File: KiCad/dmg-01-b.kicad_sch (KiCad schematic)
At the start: 64 parts, among them CN1 SCREEN, CN2 CART, CN3 EXT, P1 GND PAD, P2 GND PAD, P3 GND PAD, P4 GND PAD, SW1 POWER_SW, U1 CPU, U2 VRAM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

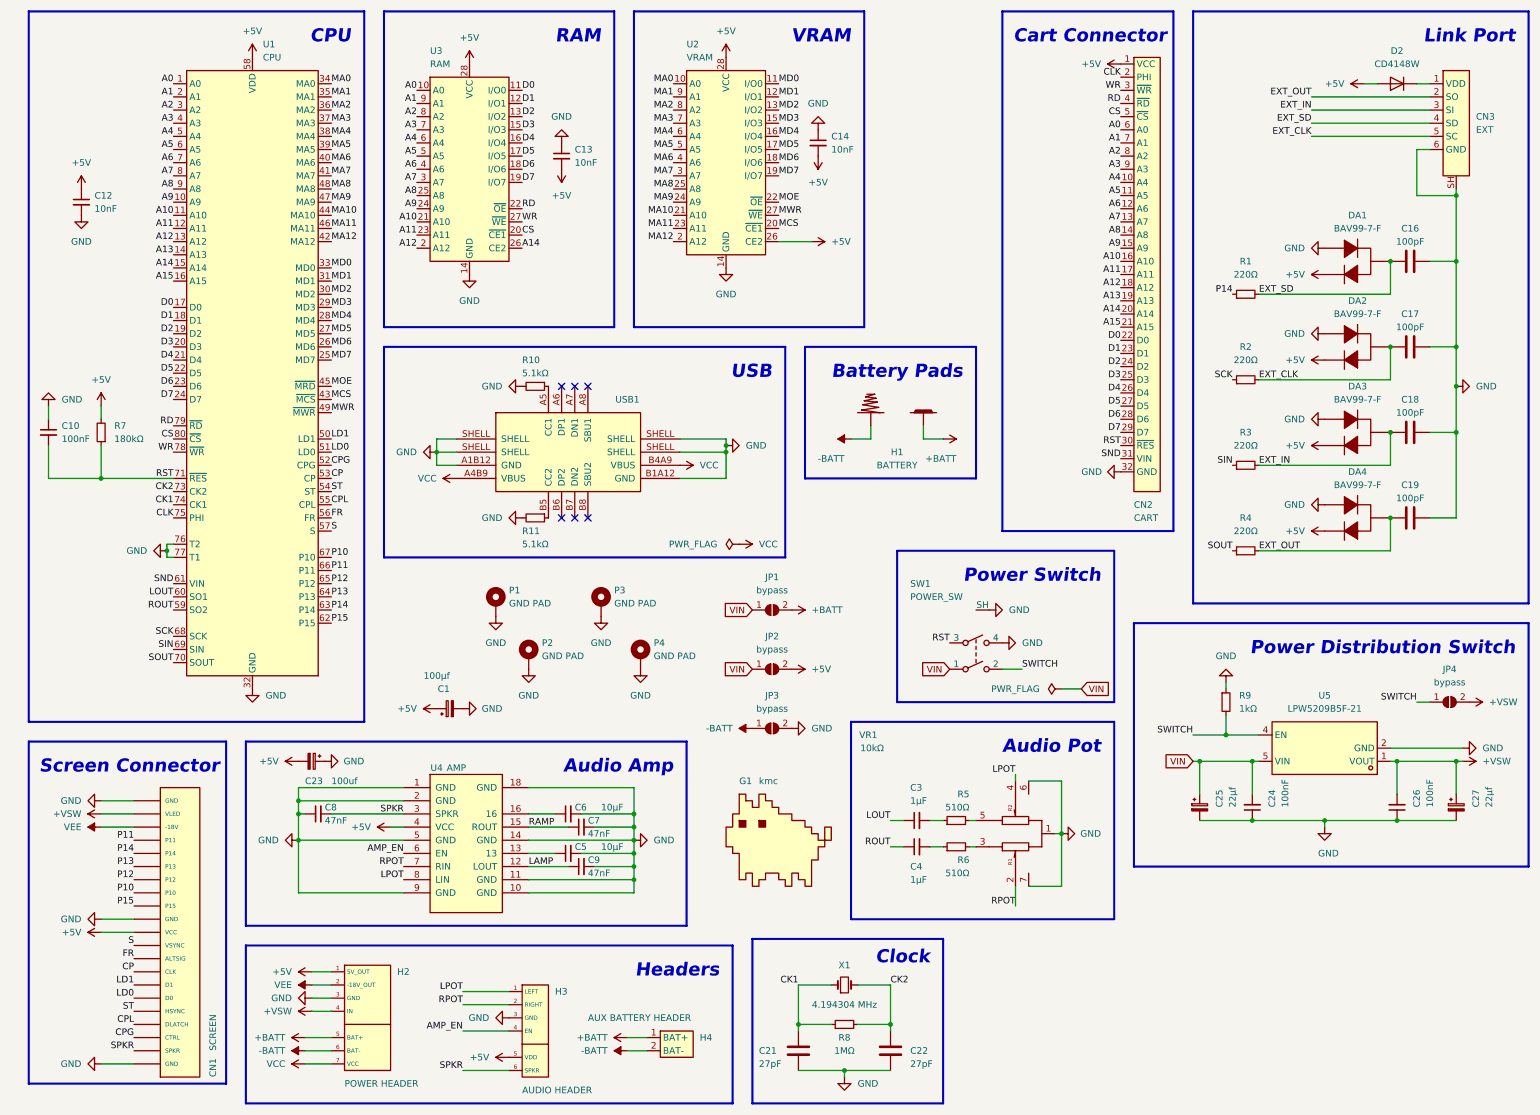
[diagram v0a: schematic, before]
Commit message: - fix c23 orientation - fix d2 footprint - minor silkscreen changes
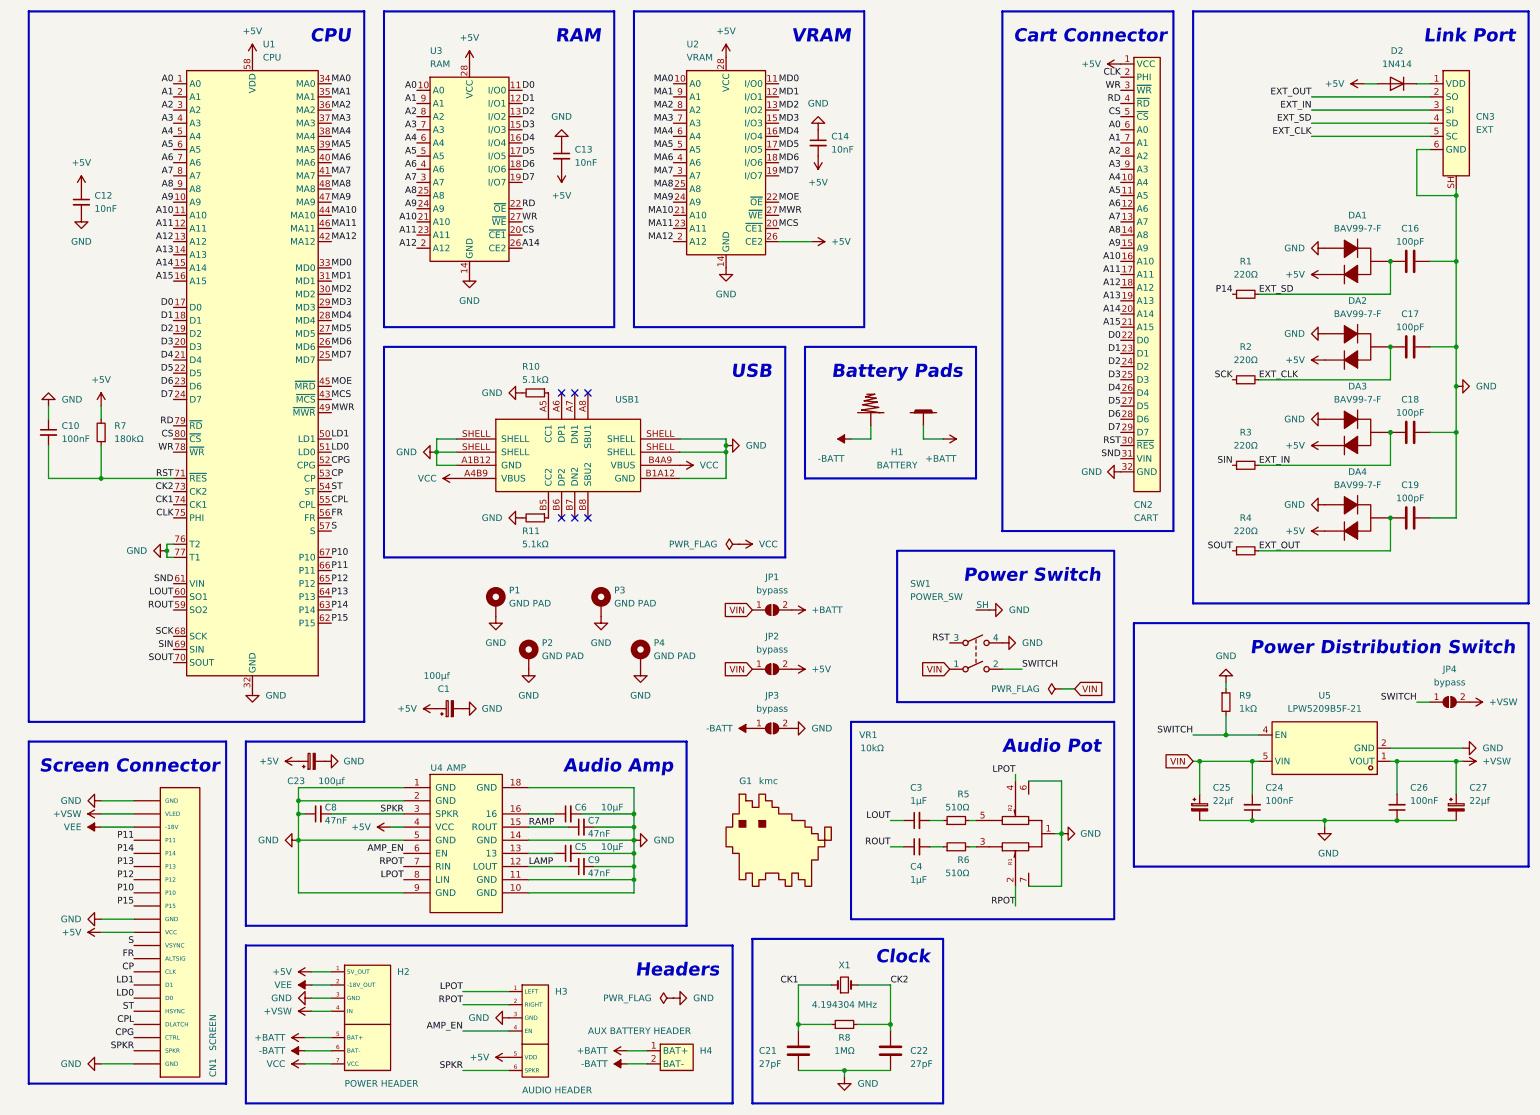
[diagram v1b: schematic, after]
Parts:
- C23: value 100uf -> 100µf
- CN1, CN2, CN3, JP1, JP2, JP3, P1, P2, P3, P4, SW1, U1, U2, U3, VR1: now left out of the parts list
- D2: value CD4148W -> 1N414; footprint Diode_SMD:D_0805_2012Metric -> Diode_SMD:D_SOD-123; symbol Diode:CD4148W -> Diode:1N4148W
- U5: footprint easyeda2kicad:SOT-23-5_L2.9-W1.6-P0.95-LS2.8-BL -> kmc_lib:SOT-23-5_L2.9-W1.6-P0.95-LS2.8-BL
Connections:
- net +5V: now also C23.1; no longer C23.2
- net GND: now also C23.2; no longer C23.1
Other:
- moved on the sheet: C23, H4, R10, USB1

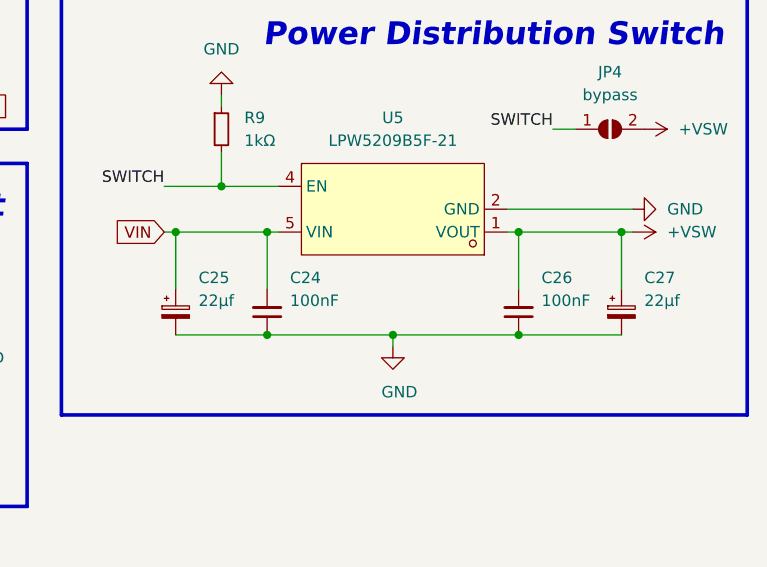
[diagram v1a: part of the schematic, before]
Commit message: remove extra power distribution switch capacitors since they were not needed
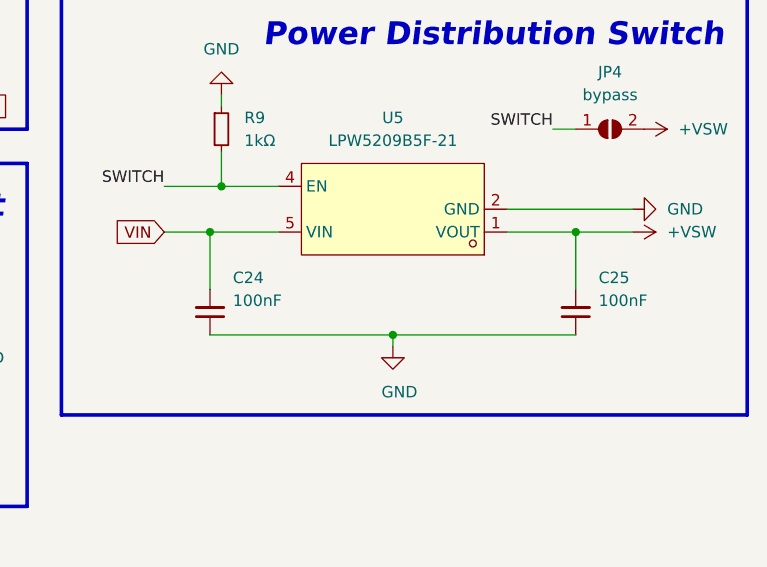
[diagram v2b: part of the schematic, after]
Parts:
- removed C25, C27: 22µf, Capacitor_Tantalum_SMD:CP_EIA-3216-18_Kemet-A_Pad1.58x1.35mm_HandSolder, symbol Device:C_Polarized_Small
- renumbered C26 to C25
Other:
- moved on the sheet: C24, C25

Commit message: update images
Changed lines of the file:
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@@
   (junction (at 290.83 87.63) (diameter 0) (color 0 0 0 0)
   )
-  (junction (at 149.86 99.06) (diameter 0) (color 0 0 0 0)
-  )
   (junction (at 132.08 182.88) (diameter 0) (color 0 0 0 0)
   )
@@
     (stroke (width 0) (type default) (color 0 0 0 0))
   )
-  (wire (pts (xy 149.86 99.06) (xy 149.86 100.33))
-    (stroke (width 0) (type default) (color 0 0 0 0))
-  )
   (wire (pts (xy 290.83 50.8) (xy 290.83 63.5))
     (stroke (width 0) (type default) (color 0 0 0 0))
@@
     (stroke (width 0) (type default) (color 0 0 0 0))
   )
-  (wire (pts (xy 149.86 99.06) (xy 149.86 97.79))
+  (wire (pts (xy 149.86 97.79) (xy 149.86 100.33))
     (stroke (width 0) (type default) (color 0 0 0 0))
   )
@@
     (pin "1")
   )
-  (symbol (lib_id "power:GND") (at 149.86 99.06 90) (unit 1)
+  (symbol (lib_id "power:GND") (at 149.86 100.33 90) (unit 1)
     (in_bom yes) (on_board yes) (fields_autoplaced)
-    (property "Reference" "#PWR0116" (id 0) (at 156.21 99.06 0)
+    (property "Reference" "#PWR0116" (id 0) (at 156.21 100.33 0)
       (effects (font (size 1.27 1.27)) hide)
     )
-    (property "Value" "GND" (id 1) (at 153.67 99.0599 90)
+    (property "Value" "GND" (id 1) (at 153.67 100.3299 90)
       (effects (font (size 1.27 1.27)) (justify right))
     )
-    (property "Footprint" "" (id 2) (at 149.86 99.06 0)
+    (property "Footprint" "" (id 2) (at 149.86 100.33 0)
       (effects (font (size 1.27 1.27)) hide)
     )
-    (property "Datasheet" "" (id 3) (at 149.86 99.06 0)
+    (property "Datasheet" "" (id 3) (at 149.86 100.33 0)
       (effects (font (size 1.27 1.27)) hide)
     )

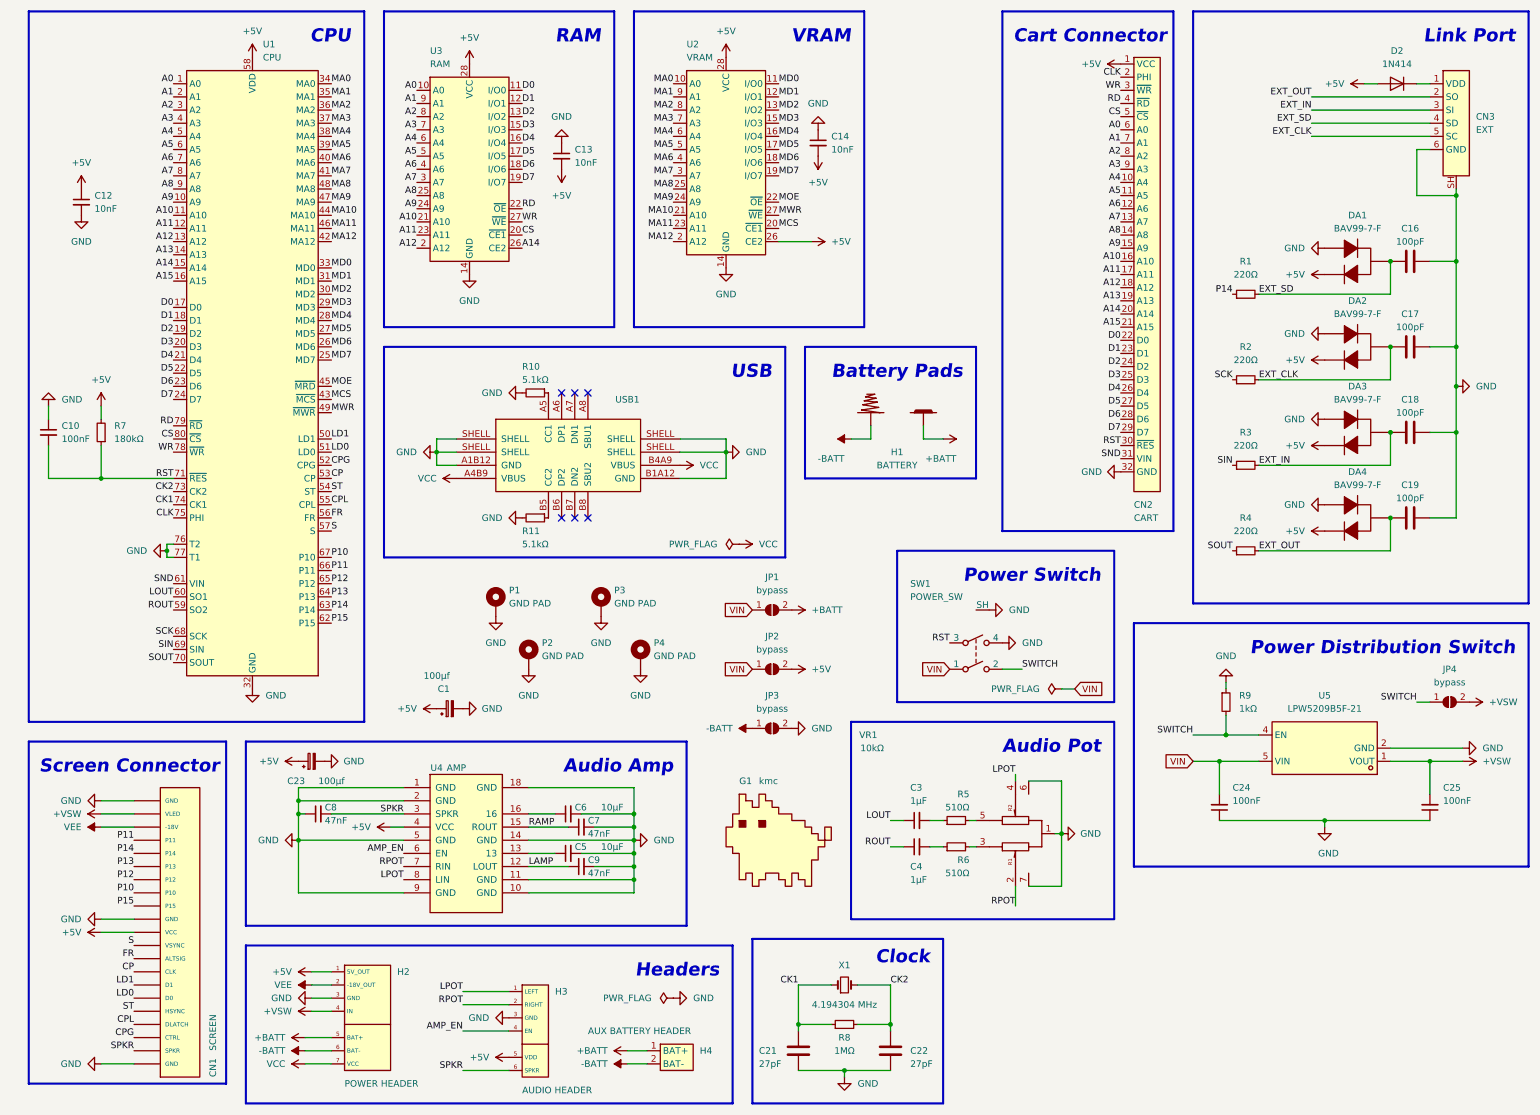
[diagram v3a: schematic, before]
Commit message: remove unused SPKR pad clean up bottom area add optional jst style connectors
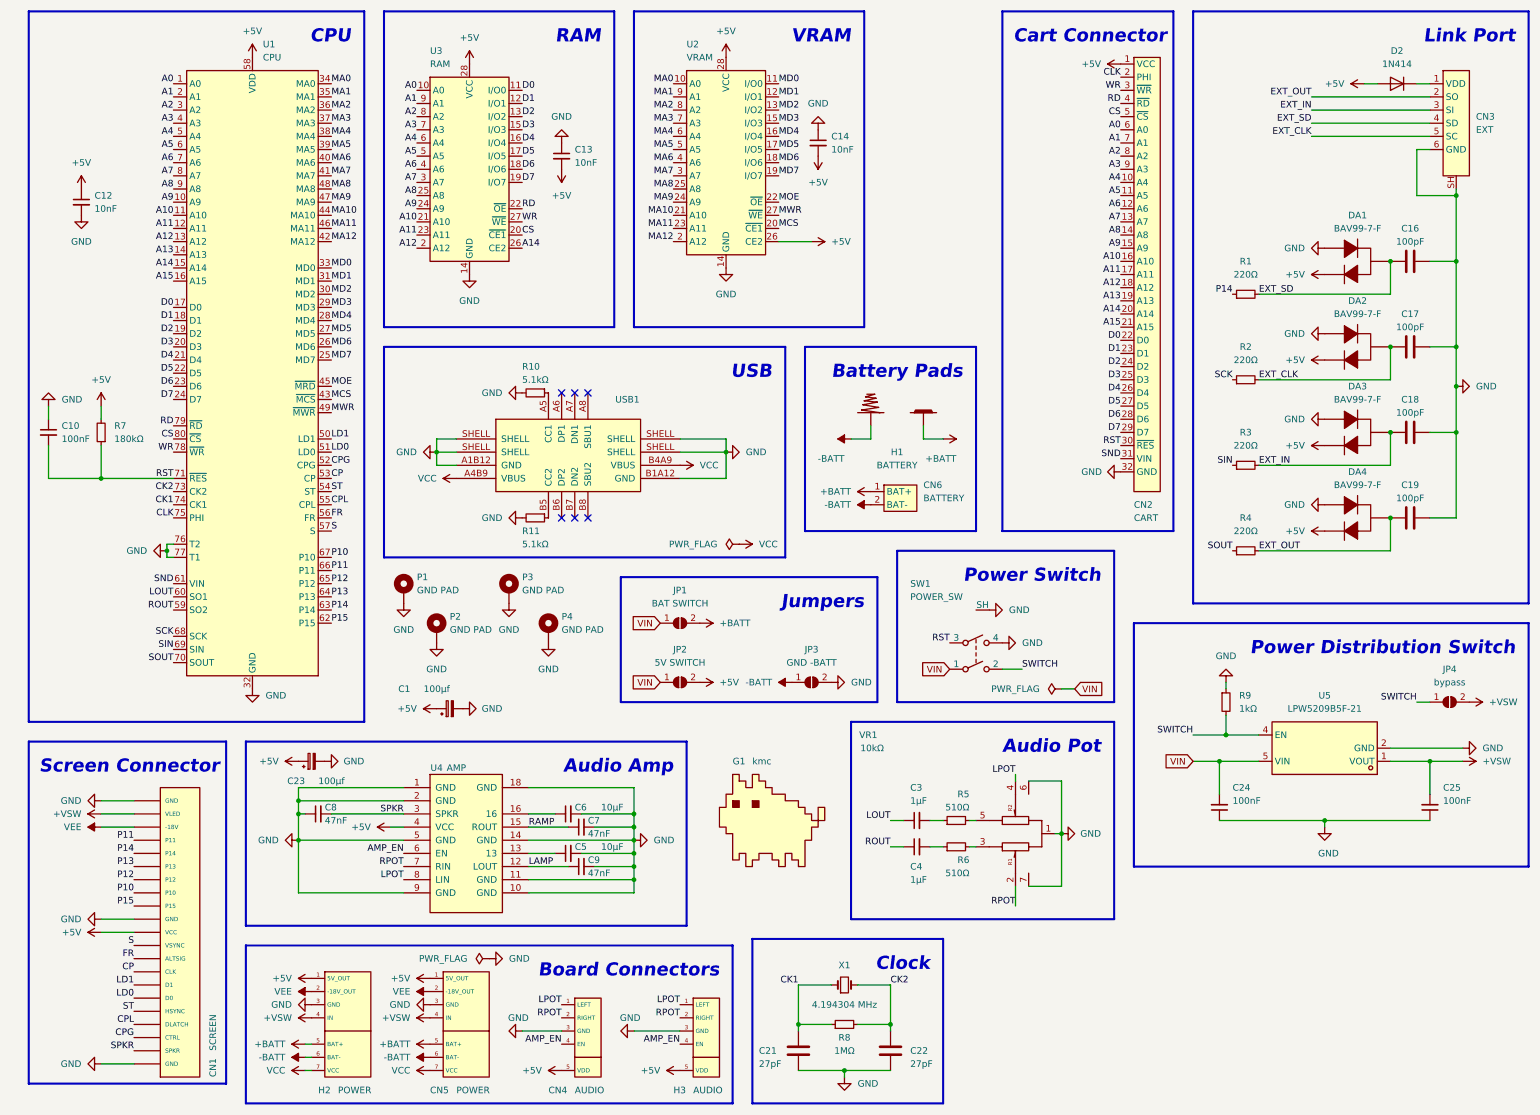
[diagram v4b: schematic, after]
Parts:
- removed H4: AUX BATTERY HEADER, kmc_lib:2.54_PAD_SMD_X2, symbol kmc_lib:DMGB_BATTERY_HEADER
- added CN4: AUDIO, easyeda2kicad:CONN-TH_5P-P1.25_HCTL_HC-1.25-5AW, symbol kmc_lib:DMGB_AUDIO_HEADER
- added CN5: POWER, easyeda2kicad:CONN-TH_7P-P1.25_HCTL_HC-1.25-7AW, symbol kmc_lib:DMGB_POWER_HEADER
- added CN6: BATTERY, easyeda2kicad:CONN-TH_2P-P1.25_HCTL_HC-1.25-2AW, symbol kmc_lib:DMGB_BATTERY_HEADER
- H2: value POWER HEADER -> POWER
- H3: value AUDIO HEADER -> AUDIO; footprint kmc_lib:2.54_PAD_SMD_X6 -> kmc_lib:2.54_PAD_SMD_X5
- JP1: value bypass -> BAT SWITCH
- JP2: value bypass -> 5V SWITCH
- JP3: value bypass -> GND -BATT
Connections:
- net +5V: now also CN4.5 (VDD), CN5.1 (5V_OUT)
- net +BATT: now also CN5.5 (BAT+), CN6.1 (BAT+)
- net +VSW: now also CN5.4 (IN)
- net -BATT: now also CN5.6 (BAT-), CN6.2 (BAT-)
- net AMP_EN: now also CN4.4 (EN)
- net GND: now also CN4.3 (GND), CN5.3 (GND)
- net LPOT: now also CN4.1 (LEFT)
- net RPOT: now also CN4.2 (RIGHT)
- net SPKR: no longer H3.6 (SPKR)
- net VCC: now also CN5.7 (VCC)
- net VEE: now also CN5.2 (-18V_OUT)
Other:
- note added: "Board Connectors"
- note added: "Jumpers"
- note removed: "Headers"
- moved on the sheet: G1, H2, JP1, JP2, JP3, P1, P2, P3, P4

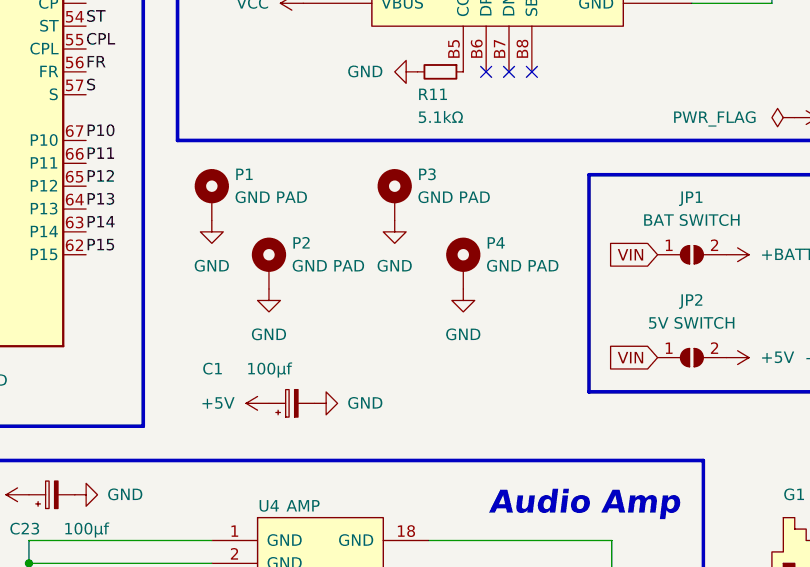
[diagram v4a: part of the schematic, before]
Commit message: test connectors (for history, to be removed)
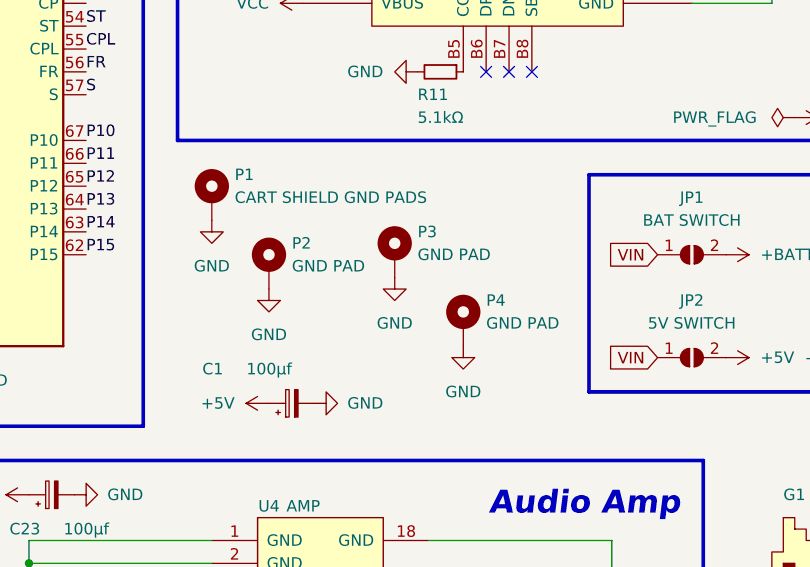
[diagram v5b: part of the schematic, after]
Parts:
- CN1: footprint kmc_lib:DMG_FPC_CONN -> dmg_lib:DMG_FPC_CONN
- CN2: footprint kmc_lib:DMG_CART_CONN -> dmg_lib:DMG_CART_CONN
- CN3: footprint kmc_lib:DMG_LINK_CONN -> dmg_lib:DMG_LINK_CONN
- H1: footprint kmc_lib:DMG_BATTERY_PADS -> dmg_lib:DMG_BATTERY_PADS
- P1: value GND PAD -> CART SHIELD GND PADS; footprint kmc_lib:DMG_CART_SHIELD_CONTACT -> dmg_lib:DMG_CART_SHIELD_CONTACT
- P2, P3, P4: footprint kmc_lib:DMG_GROUNDPAD -> dmg_lib:DMG_GROUNDPAD
- SW1: footprint kmc_lib:DMG_POWER_SWITCH -> dmg_lib:DMG_POWER_SWITCH
- U1: footprint kmc_lib:DMG_CPU -> dmg_lib:DMG_CPU
- U2, U3: footprint kmc_lib:DMG_RAM_64K -> dmg_lib:DMG_RAM_64K
- U4: footprint kmc_lib:SSOP-18_6X7.4MM_P0.8MM -> dmg_lib:DMG_AMP
- VR1: footprint kmc_lib:RES-TH_RK10J12E002L -> dmg_lib:DMG_VOLUME_POT
- X1: footprint kmc_lib:HC-49S -> dmg_lib:HC-49S
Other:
- title: DMG-01 -> DMG-01-B
- moved on the sheet: P3, P4
